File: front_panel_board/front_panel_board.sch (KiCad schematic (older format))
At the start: 8 parts, among them J1 Conn_01x02_Male, J2 Conn_02x05_Odd_Even, SW1 SW_Rotary12_Letter, SW2 SW_SPST

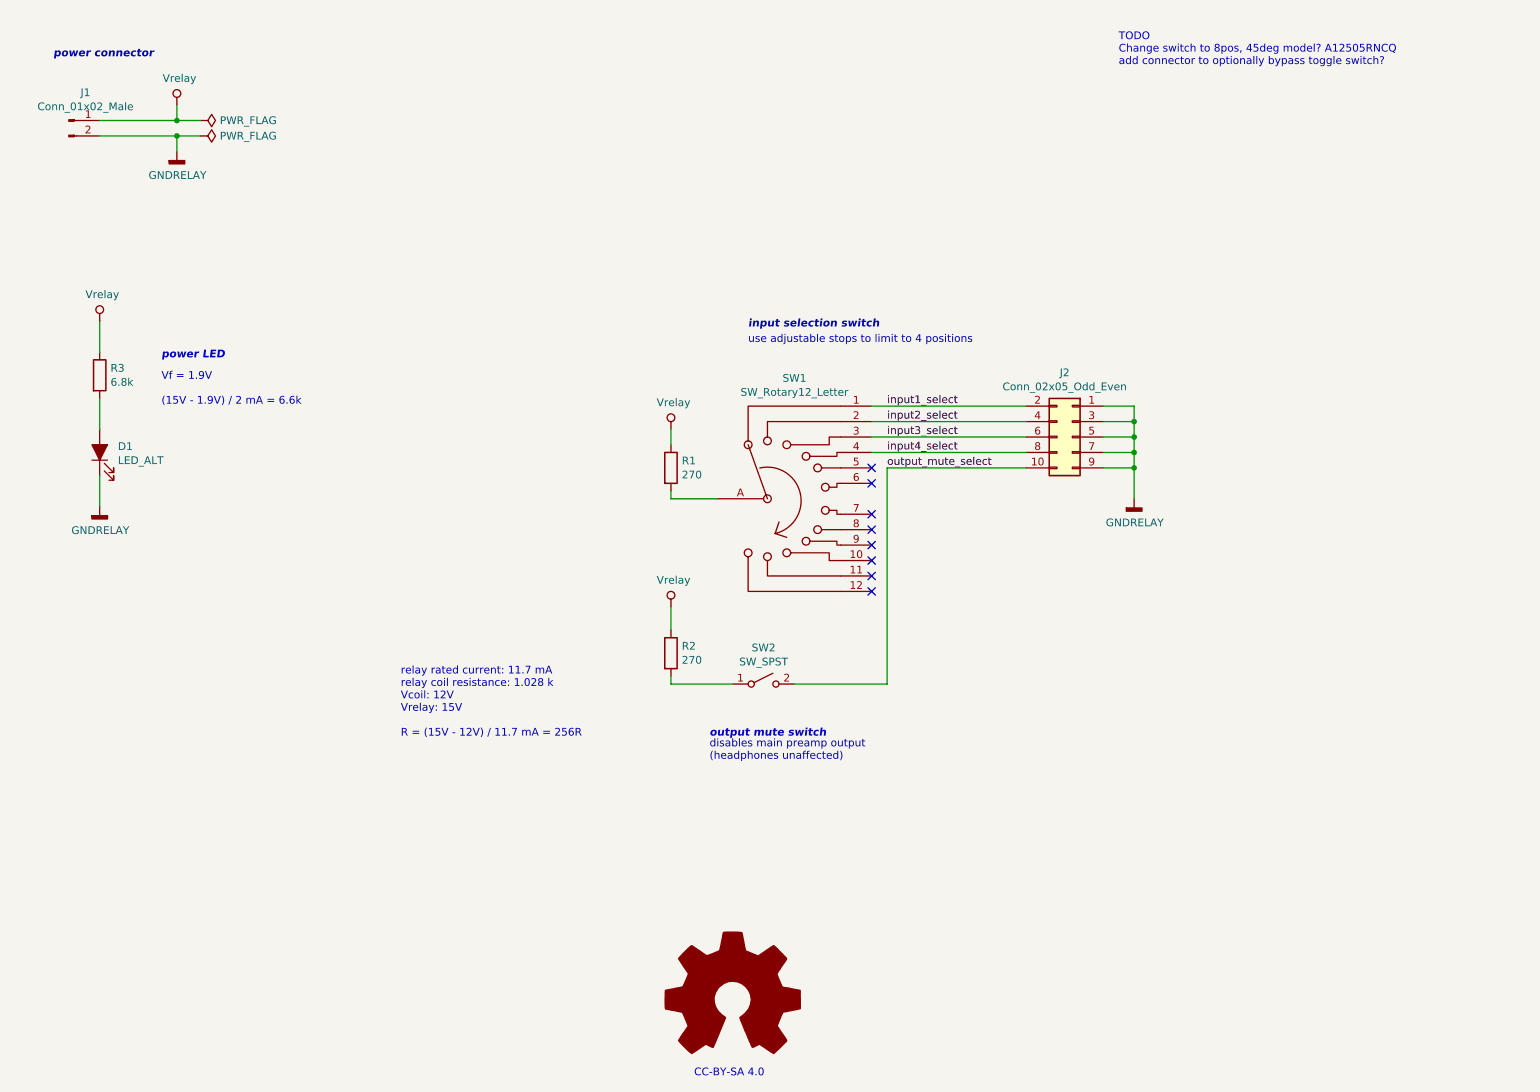
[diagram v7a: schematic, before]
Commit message: add connector to bypass mute switch and change rotary switch to 8pos model
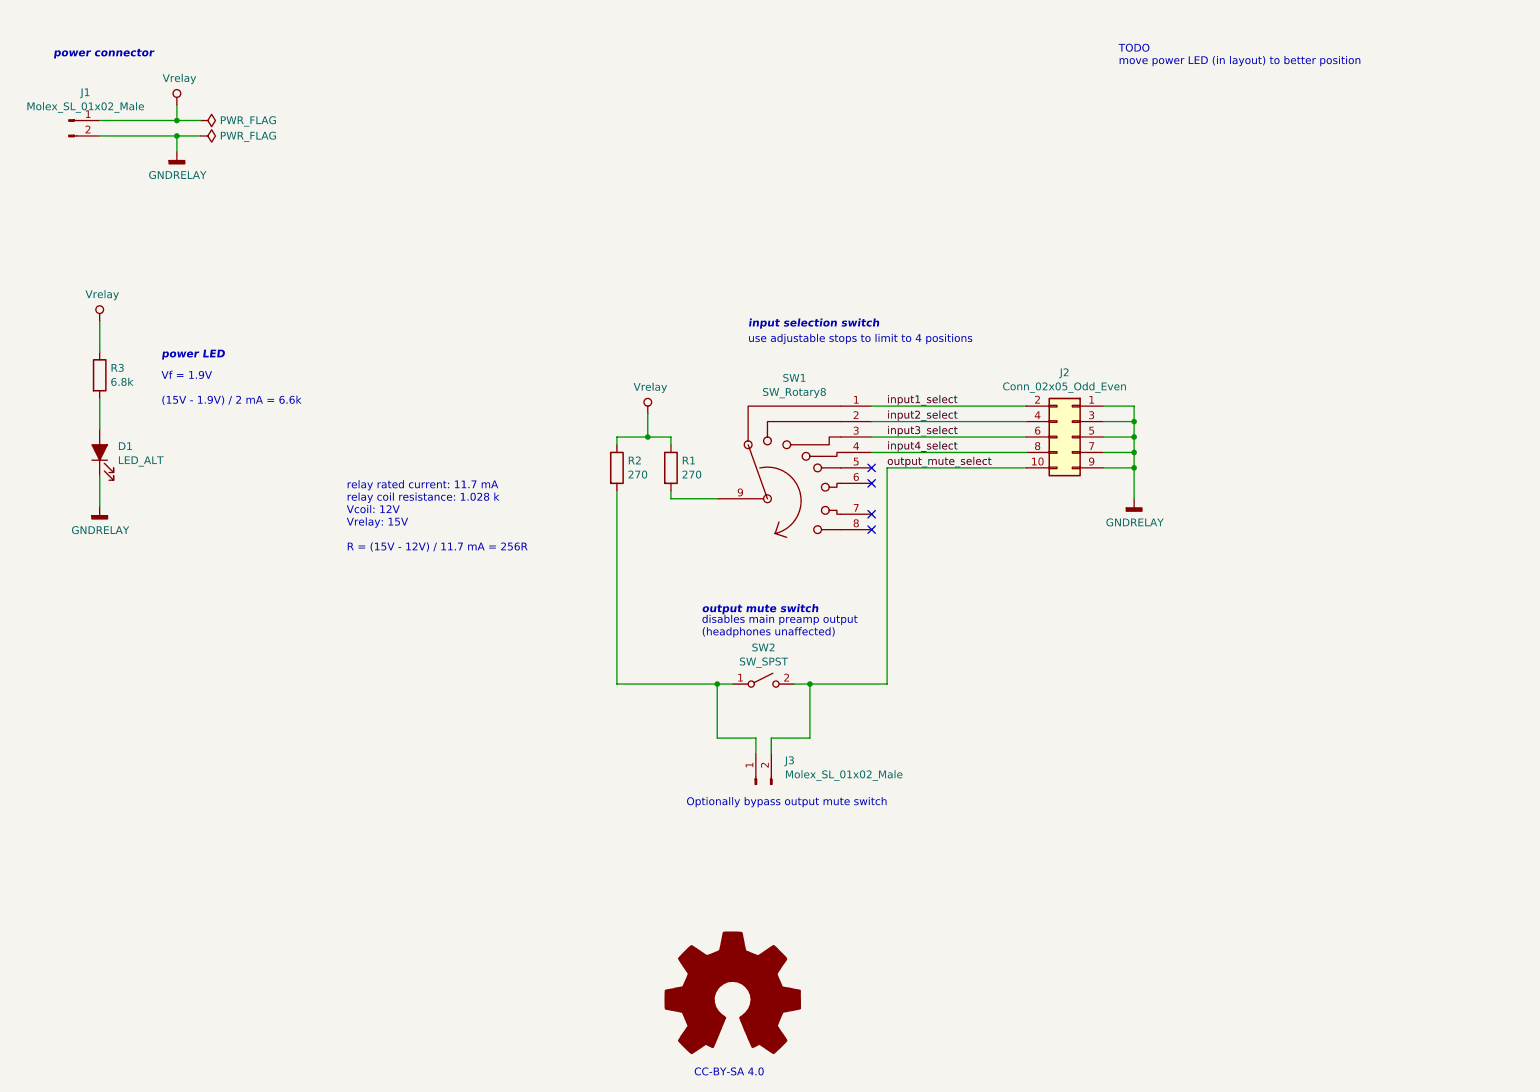
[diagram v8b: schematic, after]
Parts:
- removed J1: Conn_01x02_Male, Connector_Molex_SL:Molex_SL_A-70543-0001_1x02_P2.54mm_Vertical, symbol Connector:Conn_01x02_Male
- removed SW1: SW_Rotary12_Letter, Button_Switch_THT_gkeeth:SW_Rotary12_C&K_A112xxxxCxx, symbol Switch_gkeeth:SW_Rotary12_Letter
- added J1, J3: Molex_SL_01x02_Male, Connector_Molex_SL:Molex_SL_A-70543-0001_1x02_P2.54mm_Vertical, symbol Connector_gkeeth:Molex_SL_01x02_Male
- added SW1: SW_Rotary8, Button_Switch_THT_gkeeth:SW_Rotary8_C&K_A125xxxxCxx, symbol Switch_gkeeth:SW_Rotary8
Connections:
- net GNDRELAY: now also J1.2 (Pin_2)
- net Vrelay: now also J1.1 (Pin_1)
- net input1_select: now also SW1.1
- net input2_select: now also SW1.2
- net input3_select: now also SW1.3
- net input4_select: now also SW1.4
- net output_mute_select: now also J3.2 (Pin_2)
- net at R2.2, SW2.1 (A): now also J3.1 (Pin_1)
- net at R1.2: now also SW1.9
- no-connect marks 8 -> 4
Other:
- note added: "Optionally bypass output mute switch"
- note added: "TODO\nmove power LED (in layout) to better position"
- note removed: "TODO\nChange switch to 8pos, 45deg model? A12505RNCQ\nadd connector to optionally bypass toggle switch?"
- moved on the sheet: R2
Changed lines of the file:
@@
 $EndDescr
-$Comp
-L Connector:Conn_01x02_Male J1
-U 1 1 5D13901D
-P 1200 1450
-F 0 "J1" H 1308 1631 50  0000 C CNN
-F 1 "Conn_01x02_Male" H 1308 1540 50  0000 C CNN
-F 2 "Connector_Molex_SL:Molex_SL_A-70543-0001_1x02_P2.54mm_Vertical" H 1200 1450 50  0001 C CNN
-F 3 "~" H 1200 1450 50  0001 C CNN
-	1    1200 1450
-	1    0    0    -1
-$EndComp
 $Comp
 L Device:LED_ALT D1
@@
 input4_select
 Wire Wire Line
-	5900 5100 6500 5100
+	5900 5100 6000 5100
 Wire Wire Line
 	6500 3700 7400 3700
@@
 L power_gkeeth:Vrelay #PWR0103
 U 1 1 5CD2F453
-P 5100 3450
-F 0 "#PWR0103" H 5100 3300 50  0001 C CNN
-F 1 "Vrelay" H 5117 3623 50  0000 C CNN
-F 2 "" H 5100 3450 50  0001 C CNN
-F 3 "" H 5100 3450 50  0001 C CNN
-	1    5100 3450
+P 4950 3350
+F 0 "#PWR0103" H 4950 3200 50  0001 C CNN
+F 1 "Vrelay" H 4967 3523 50  0000 C CNN
+F 2 "" H 4950 3350 50  0001 C CNN
+F 3 "" H 4950 3350 50  0001 C CNN
+	1    4950 3350
 	1    0    0    -1
 $EndComp
@@
 	5100 3900 5400 3900
 Wire Wire Line
-	5100 3550 5100 3450
-$Comp
-L power_gkeeth:Vrelay #PWR0104
-U 1 1 5CD3104E
-P 5100 4600
-F 0 "#PWR0104" H 5100 4450 50  0001 C CNN
-F 1 "Vrelay" H 5117 4773 50  0000 C CNN
-F 2 "" H 5100 4600 50  0001 C CNN
-F 3 "" H 5100 4600 50  0001 C CNN
-	1    5100 4600
-	1    0    0    -1
-$EndComp
-Wire Wire Line
-	5100 5050 5100 5100
-Wire Wire Line
-	5100 5100 5500 5100
-Wire Wire Line
-	5100 4750 5100 4600
-Text Notes 5350 5600 0    50   ~ 0
+	5100 3500 4950 3500
+Wire Wire Line
+	4750 3850 4750 5100
+Wire Wire Line
+	4750 3550 4750 3500
+Text Notes 5300 4800 0    50   ~ 0
 disables main preamp output\n(headphones unaffected)
-Text Notes 5350 5450 0    50   Italic 10
+Text Notes 5300 4650 0    50   Italic 10
 output mute switch
 Text Notes 5600 2800 0    50   Italic 10
@@
 	1900 1450 2050 1450
 Connection ~ 1900 1450
-$Comp
-L Switch_gkeeth:SW_Rotary12_Letter SW1
-U 1 1 5CD4AABC
-P 6000 3900
-F 0 "SW1" H 5900 4681 50  0000 C CNN
-F 1 "SW_Rotary12_Letter" H 5900 4590 50  0000 C CNN
-F 2 "Button_Switch_THT_gkeeth:SW_Rotary12_C&K_A112xxxxCxx" H 5800 4600 50  0001 C CNN
-F 3 "http://cdn-reichelt.de/documents/datenblatt/C200/DS-Serie%23LOR.pdf" H 5800 4600 50  0001 C CNN
-	1    6000 3900
-	1    0    0    -1
-$EndComp
 NoConn ~ 6400 3700
 NoConn ~ 6400 3800
 NoConn ~ 6400 4000
 NoConn ~ 6400 4100
-NoConn ~ 6400 4200
-NoConn ~ 6400 4300
-NoConn ~ 6400 4400
-NoConn ~ 6400 4500
 Wire Wire Line
 	6500 3700 6500 5100
 Text Notes 5600 2900 0    50   ~ 0
 use adjustable stops to limit to 4 positions
-Text Notes 3350 5450 0    50   ~ 0
+Text Notes 3000 4250 0    50   ~ 0
 relay rated current: 11.7 mA\nrelay coil resistance: 1.028 k\nVcoil: 12V\nVrelay: 15V\n\nR = (15V - 12V) / 11.7 mA = 256R
 $Comp
 L Device:R R2
 U 1 1 5CD172C4
-P 5100 4900
-F 0 "R2" H 5170 4946 50  0000 L CNN
-F 1 "270" H 5170 4855 50  0000 L CNN
-F 2 "Resistor_SMD:R_0603_1608Metric_Pad1.05x0.95mm_HandSolder" V 5030 4900 50  0001 C CNN
-F 3 "http://www.yageo.com/documents/recent/PYu-RT_1-to-0.01_RoHS_L_9.pdf" H 5100 4900 50  0001 C CNN
-F 4 "Yageo" H 5100 4900 50  0001 C CNN "Manufacturer"
-F 5 "RT0603DRE07270RL" H 5100 4900 50  0001 C CNN "Manufacturer PN"
-F 6 "Digikey" H 5100 4900 50  0001 C CNN "Distributor"
-F 7 "311-2504-1-ND" H 5100 4900 50  0001 C CNN "Distributor PN"
-F 8 "https://www.digikey.com/product-detail/en/yageo/RT0603DRE07270RL/311-2504-1-ND/6128923" H 5100 4900 50  0001 C CNN "URL"
-F 9 "0.12" H 5100 4900 50  0001 C CNN "Unit Price"
-	1    5100 4900
+P 4750 3700
+F 0 "R2" H 4820 3746 50  0000 L CNN
+F 1 "270" H 4820 3655 50  0000 L CNN
+F 2 "Resistor_SMD:R_0603_1608Metric_Pad1.05x0.95mm_HandSolder" V 4680 3700 50  0001 C CNN
+F 3 "http://www.yageo.com/documents/recent/PYu-RT_1-to-0.01_RoHS_L_9.pdf" H 4750 3700 50  0001 C CNN
+F 4 "Yageo" H 4750 3700 50  0001 C CNN "Manufacturer"
+F 5 "RT0603DRE07270RL" H 4750 3700 50  0001 C CNN "Manufacturer PN"
+F 6 "Digikey" H 4750 3700 50  0001 C CNN "Distributor"
+F 7 "311-2504-1-ND" H 4750 3700 50  0001 C CNN "Distributor PN"
+F 8 "https://www.digikey.com/product-detail/en/yageo/RT0603DRE07270RL/311-2504-1-ND/6128923" H 4750 3700 50  0001 C CNN "URL"
+F 9 "0.12" H 4750 3700 50  0001 C CNN "Unit Price"
+	1    4750 3700
 	1    0    0    -1
 $EndComp
@@
 Vf = 1.9V\n\n(15V - 1.9V) / 2 mA = 6.6k
 Text Notes 8000 1100 0    50   ~ 0
-TODO\nChange switch to 8pos, 45deg model? A12505RNCQ\nadd connector to optionally bypass toggle switch?
+TODO\nmove power LED (in layout) to better position
 $Comp
 L Graphic:Logo_Open_Hardware_Large #LOGO?
@@
 Text Notes 5250 7650 0    50   ~ 0
 CC-BY-SA 4.0
+$Comp
+L Switch_gkeeth:SW_Rotary8 SW1
+U 1 1 5D180485
+P 6000 3900
+F 0 "SW1" H 5900 4681 50  0000 C CNN
+F 1 "SW_Rotary8" H 5900 4590 50  0000 C CNN
+F 2 "Button_Switch_THT_gkeeth:SW_Rotary8_C&K_A125xxxxCxx" H 5800 4600 50  0001 C CNN
+F 3 "" H 5800 4600 50  0001 C CNN
+F 4 "C&K" H 6000 3900 50  0001 C CNN "Manufacturer"
+F 5 "A11205RNCQ" H 6000 3900 50  0001 C CNN "Manufacturer PN"
+	1    6000 3900
+	1    0    0    -1
+$EndComp
+$Comp
+L Connector_gkeeth:Molex_SL_01x02_Male J3
+U 1 1 5D183CB3
+P 5650 5750
+F 0 "J3" V 5804 5562 50  0000 R CNN
+F 1 "Molex_SL_01x02_Male" V 5713 5562 50  0000 R CNN
+F 2 "Connector_Molex_SL:Molex_SL_A-70543-0001_1x02_P2.54mm_Vertical" H 5650 5750 50  0001 C CNN
+F 3 "https://www.molex.com/pdm_docs/sd/705430001_sd.pdf" H 5650 5750 50  0001 C CNN
+	1    5650 5750
+	0    -1   -1   0
+$EndComp
+Wire Wire Line
+	4950 3500 4750 3500
+Connection ~ 4950 3500
+Wire Wire Line
+	4950 3500 4950 3350
+Wire Wire Line
+	5100 3550 5100 3500
+Wire Wire Line
+	5750 5550 5750 5450
+Wire Wire Line
+	5750 5450 6000 5450
+Wire Wire Line
+	6000 5450 6000 5100
+Connection ~ 6000 5100
+Wire Wire Line
+	6000 5100 6500 5100
+Wire Wire Line
+	4750 5100 5400 5100
+Wire Wire Line
+	5650 5550 5650 5450
+Wire Wire Line
+	5650 5450 5400 5450
+Wire Wire Line
+	5400 5450 5400 5100
+Connection ~ 5400 5100
+Wire Wire Line
+	5400 5100 5500 5100
+Text Notes 5200 5900 0    50   ~ 0
+Optionally bypass output mute switch
+$Comp
+L Connector_gkeeth:Molex_SL_01x02_Male J1
+U 1 1 5D18B97E
+P 1200 1450
+F 0 "J1" H 1308 1631 50  0000 C CNN
+F 1 "Molex_SL_01x02_Male" H 1308 1540 50  0000 C CNN
+F 2 "Connector_Molex_SL:Molex_SL_A-70543-0001_1x02_P2.54mm_Vertical" H 1200 1450 50  0001 C CNN
+F 3 "https://www.molex.com/pdm_docs/sd/705430001_sd.pdf" H 1200 1450 50  0001 C CNN
+	1    1200 1450
+	1    0    0    -1
+$EndComp
 $EndSCHEMATC
